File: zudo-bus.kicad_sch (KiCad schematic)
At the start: 56 parts, among them P1 WJ500V-5.08-2P-14-00A, P2 WJ500V-5.08-2P-14-00A, U10 2541WR-2X08P, U11 2541WR-2X08P, U12 1217754-1, U13 1217754-1, U14 1217754-1, U15 1217754-1, U2 2541WR-2X08P, U3 YLED0603YG, U4 NCD1608A1, U5 2541WR-2X08P, U6 2541WR-2X08P, U7 2541WR-2X08P, U8 2541WR-2X08P, U9 2541WR-2X08P

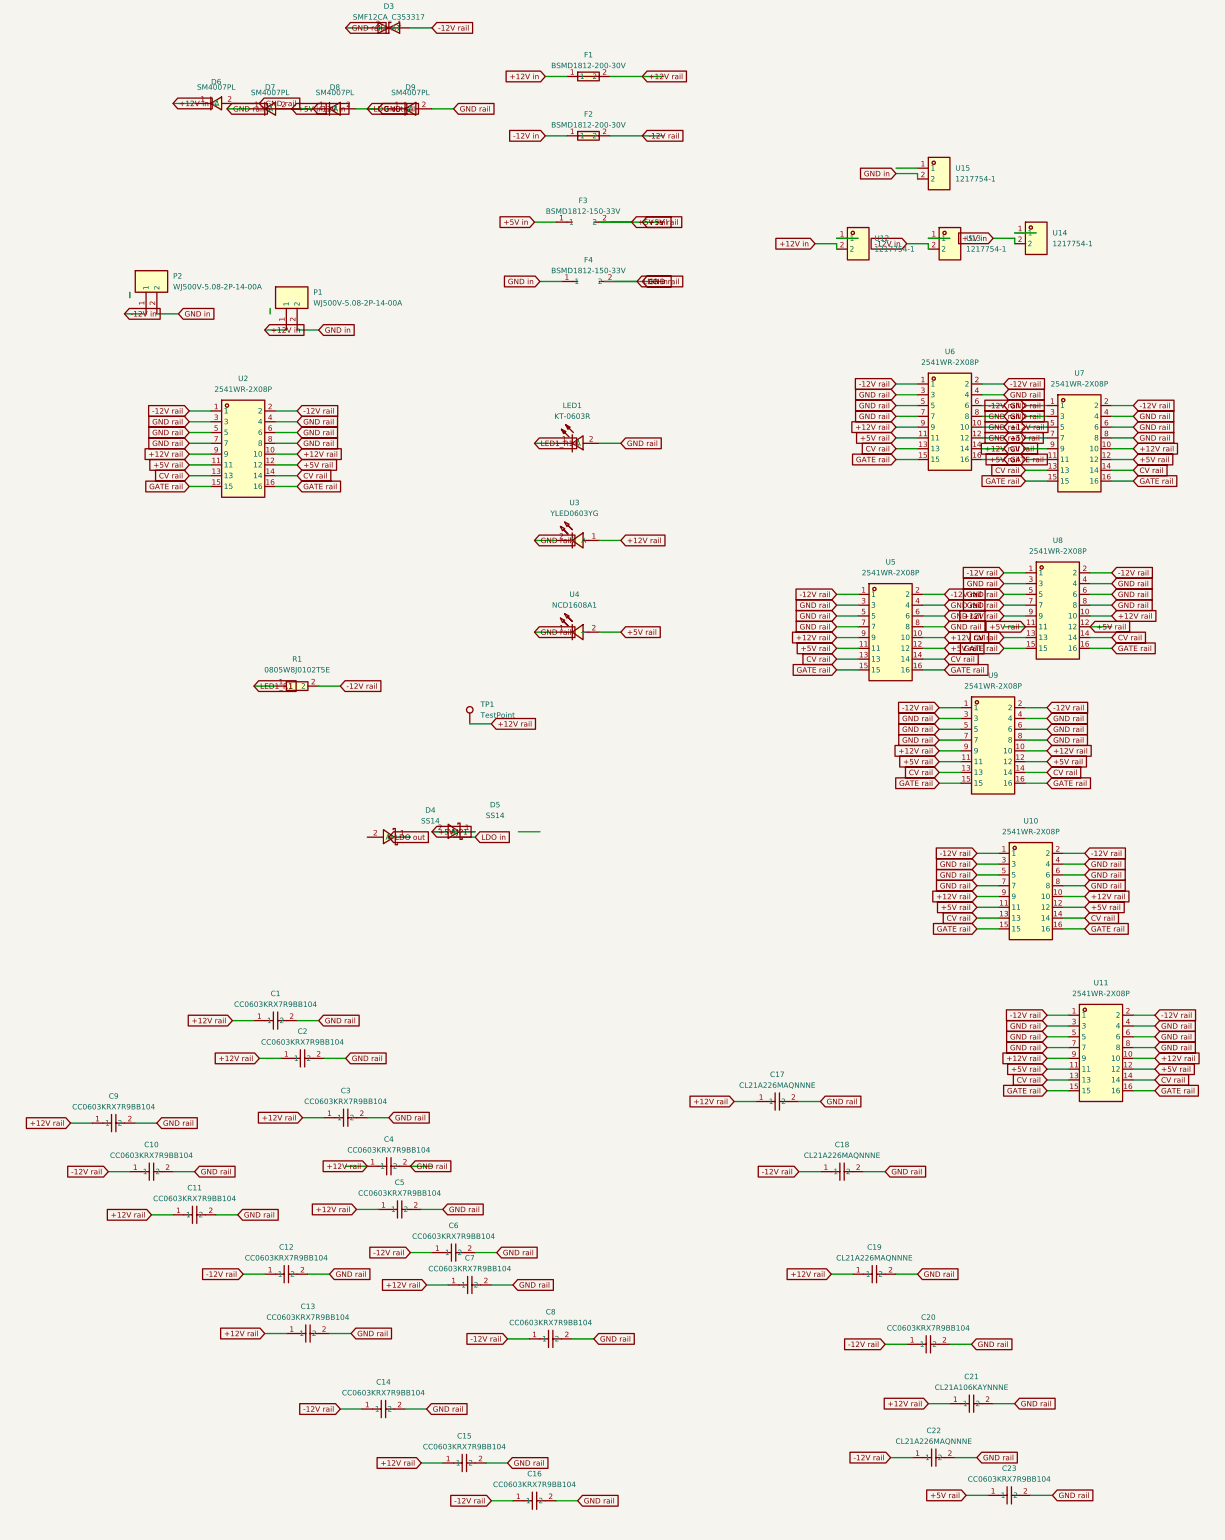
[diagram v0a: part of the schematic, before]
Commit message: Remove P1 GND in label for user to recreate in KiCad
Deleted the P1 GND in label that was displaying incorrectly.
User will recreate it in KiCad GUI like they did for P2.
Wire at (78.74, 57.15) to (83.82, 57.15) remains for reconnection.

Co-Authored-By: Claude Opus 4.5 <noreply@anthropic.com>
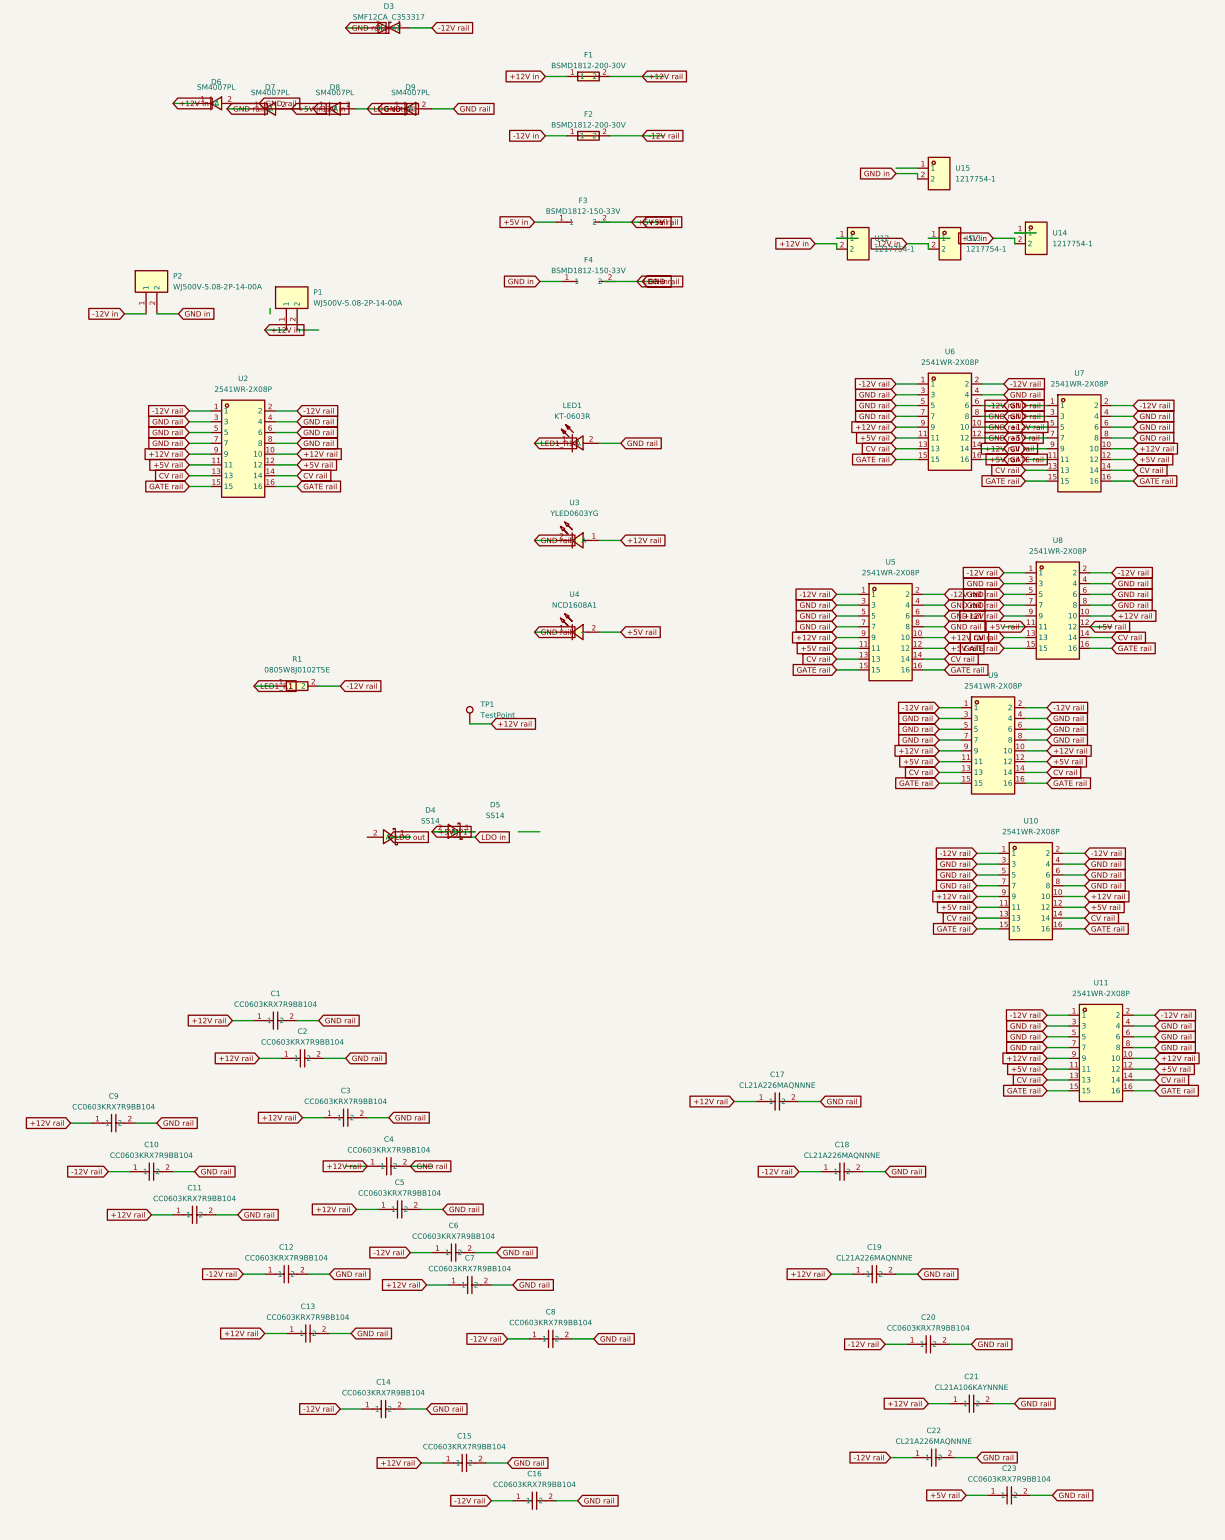
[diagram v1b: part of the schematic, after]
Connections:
- net +5V rail: no longer F3.2
- net GND in: no longer P1.2
- net GND rail: no longer F4.2

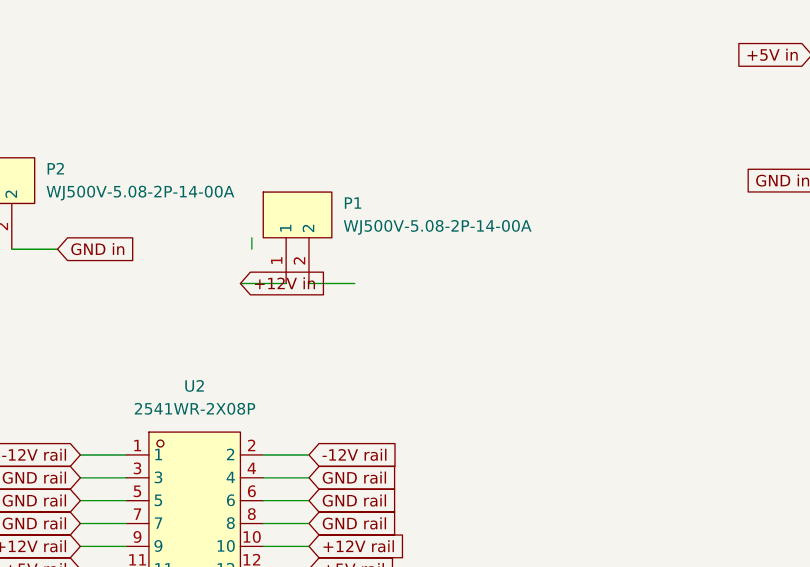
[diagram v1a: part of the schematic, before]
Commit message: Add P1 GND in label matching P2's working format
Added GND in label at (83.82, 57.15, 0) with:
- rotation 0
- justify left
- Intersheetrefs at (78.74, 57.15, 0)

Exact same format as P2's working GND in label.

Co-Authored-By: Claude Opus 4.5 <noreply@anthropic.com>
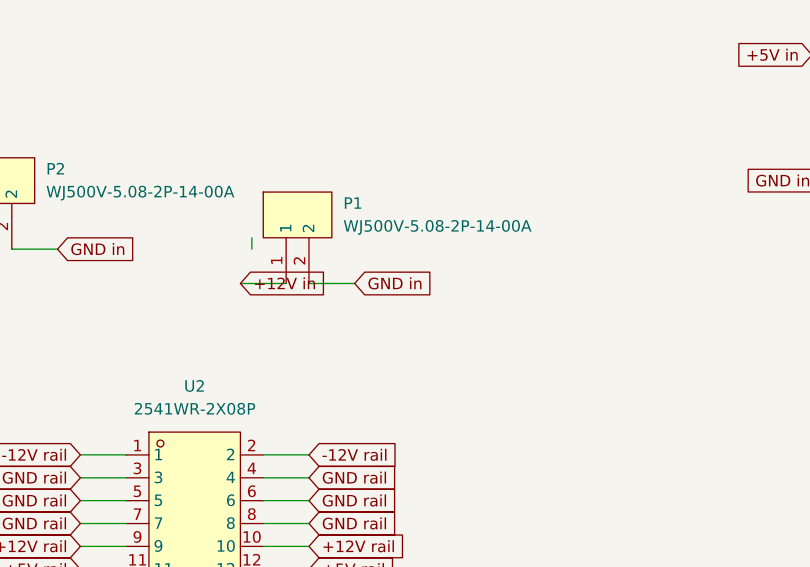
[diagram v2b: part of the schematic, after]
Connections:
- net GND in: now also P1.2
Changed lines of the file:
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@@
+		)
+	)
+	(global_label "GND in"
+		(shape input)
+		(at 83.82 57.15 0)
+		(effects
+			(font
+				(size 1.27 1.27)
+			)
+			(justify left)
+		)
+		(property "Intersheetrefs" "${INTERSHEET_REFS}"
+			(at 78.74 57.15 0)
+			(effects
+				(font
+					(size 1.27 1.27)
+				)
+				(hide yes)
+			)
 		)
 	)
